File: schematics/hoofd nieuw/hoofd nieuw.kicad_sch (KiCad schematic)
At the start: 21 parts, among them J1 Conn_01x04_Pin

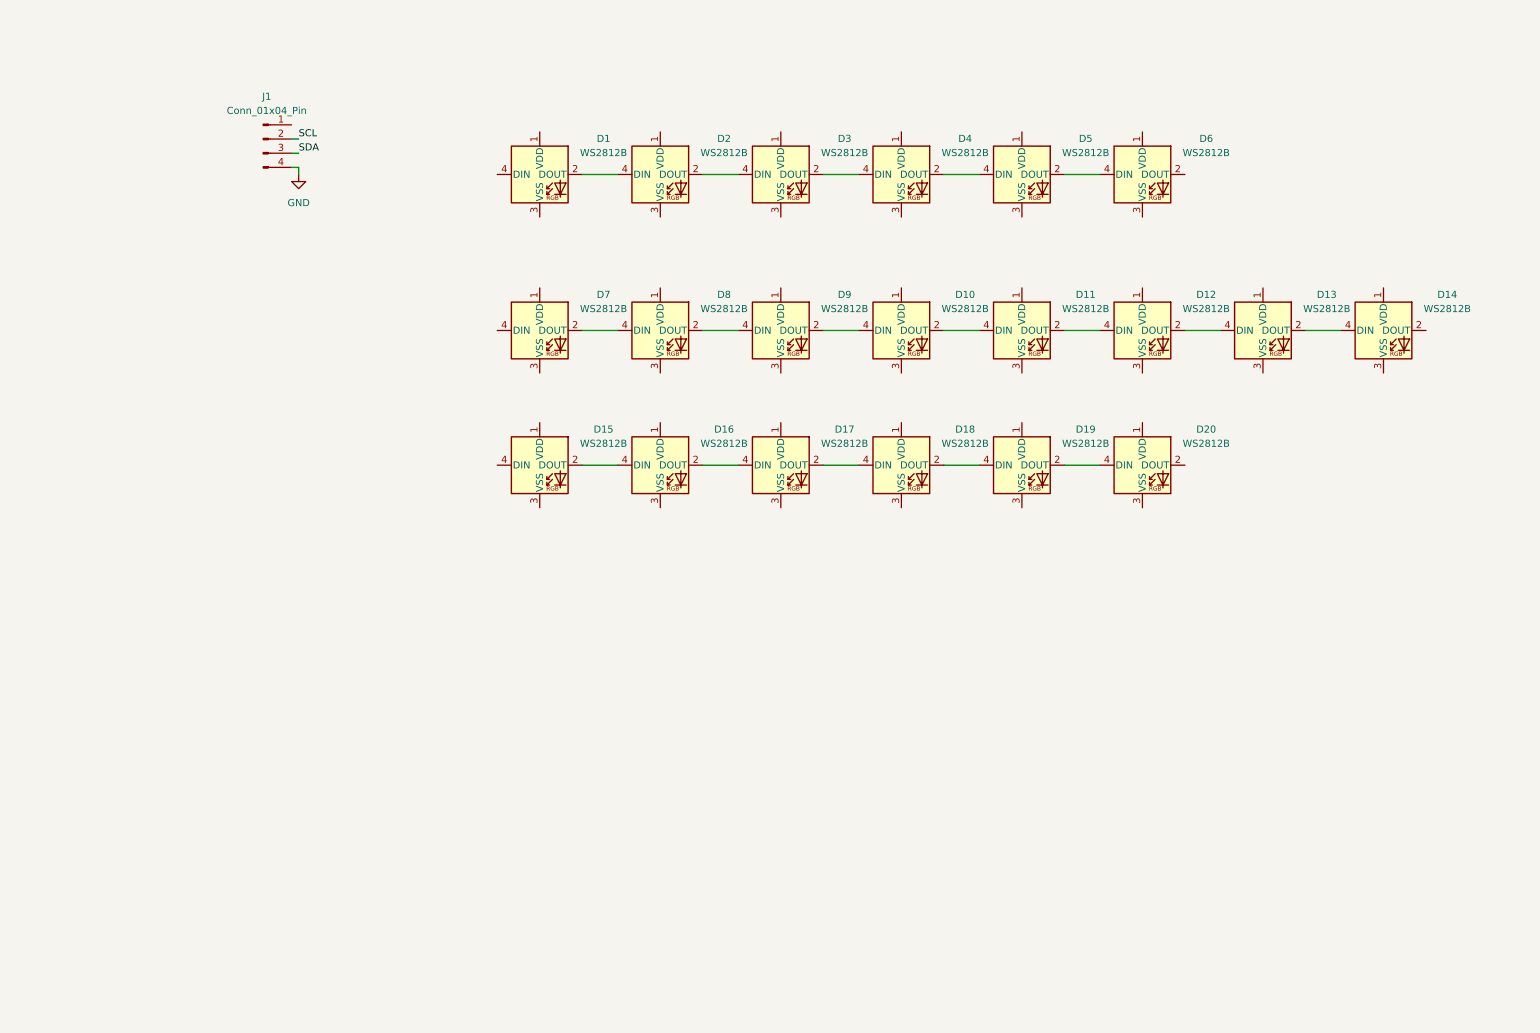
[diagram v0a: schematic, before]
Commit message: schema geupdate voor ATtiny 202 (nog niet af)
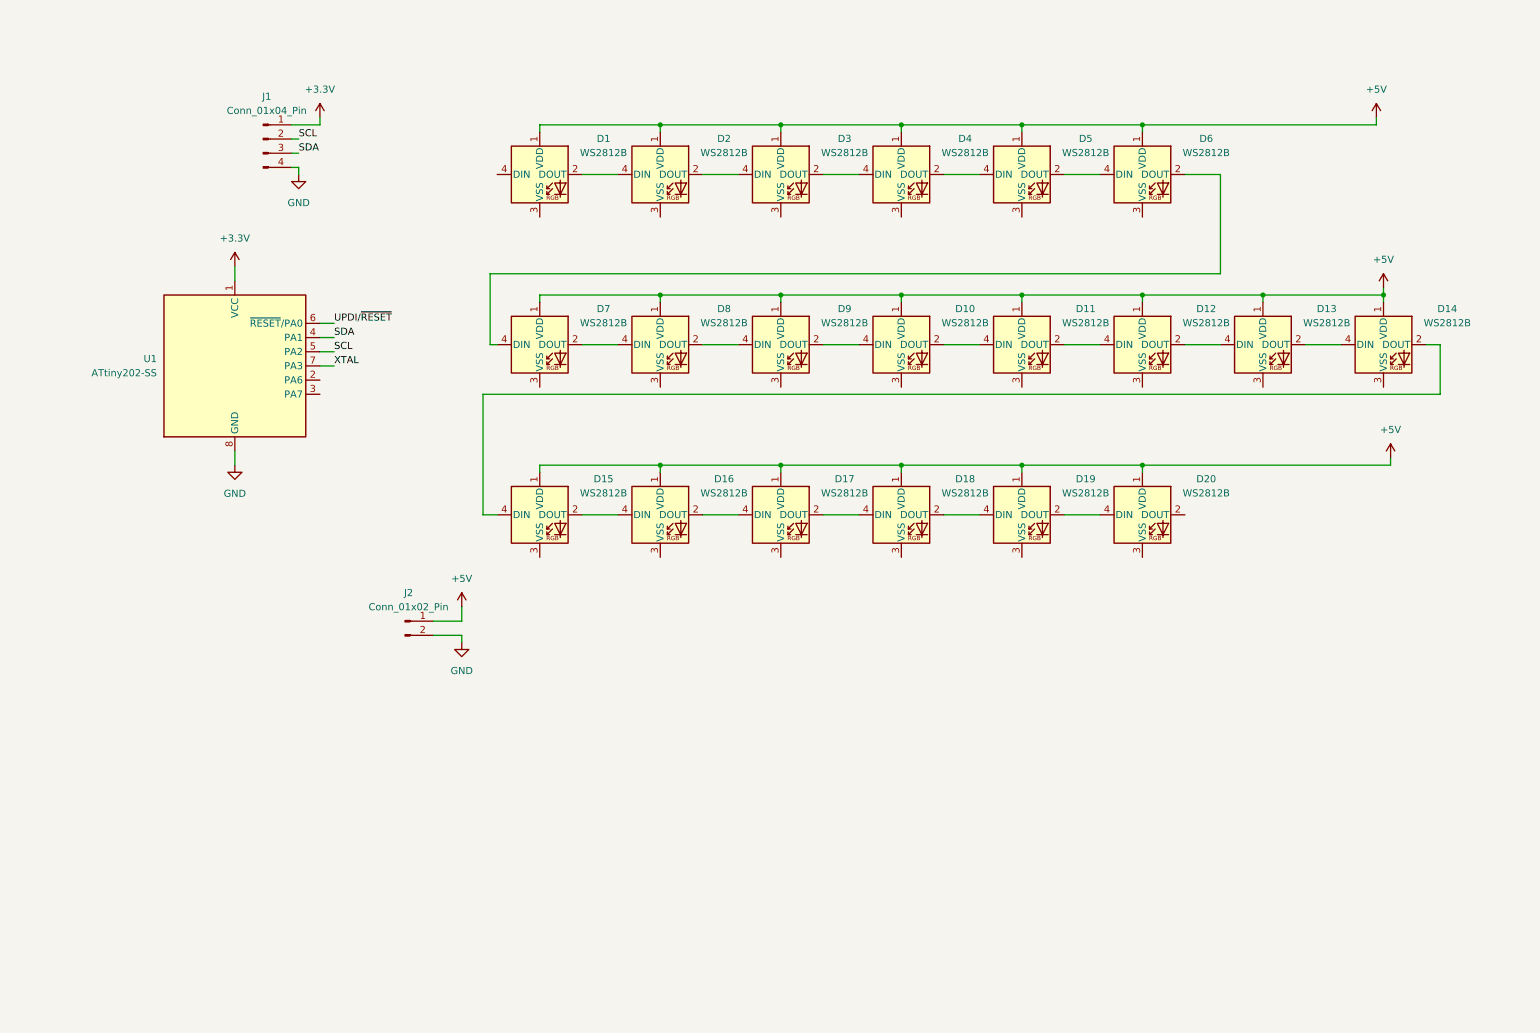
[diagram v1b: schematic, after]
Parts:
- added J2: Conn_01x02_Pin, symbol Connector:Conn_01x02_Pin
- added U1: ATtiny202-SS, Package_SO:SOIC-8_3.9x4.9mm_P1.27mm, symbol MCU_Microchip_ATtiny:ATtiny202-SS
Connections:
- net GND: now also J2.2 (Pin_2), U1.8 (GND)
- net SCL: now also U1.5 (PA2)
- net SDA: now also U1.4 (PA1)
- net +5V: now reaches D9.1 (VDD)
- net +5V: now also D1.1 (VDD), D10.1 (VDD), D11.1 (VDD), D12.1 (VDD), D13.1 (VDD), D14.1 (VDD), D15.1 (VDD), D16.1 (VDD), D17.1 (VDD), D18.1 (VDD), D19.1 (VDD), D2.1 (VDD), D20.1 (VDD), D3.1 (VDD), D4.1 (VDD), D5.1 (VDD), D6.1 (VDD), D7.1 (VDD), D8.1 (VDD), J2.1 (Pin_1)
- net at D15.4 (DIN): now also D14.2 (DOUT)
- net +3.3V: now reaches J1.1 (Pin_1)
- net +3.3V: now also U1.1 (VCC)
- net at D6.2 (DOUT): now also D7.4 (DIN)
- new net UPDI/~{RESET}: U1.6 (~{RESET}/PA0)
- new net XTAL: U1.7 (PA3)
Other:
- moved on the sheet: D10, D11, D12, D13, D14, D15, D16, D17, D18, D19, D20, D7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

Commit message: schema bijna klaar allen nog SRF02 toevoegen
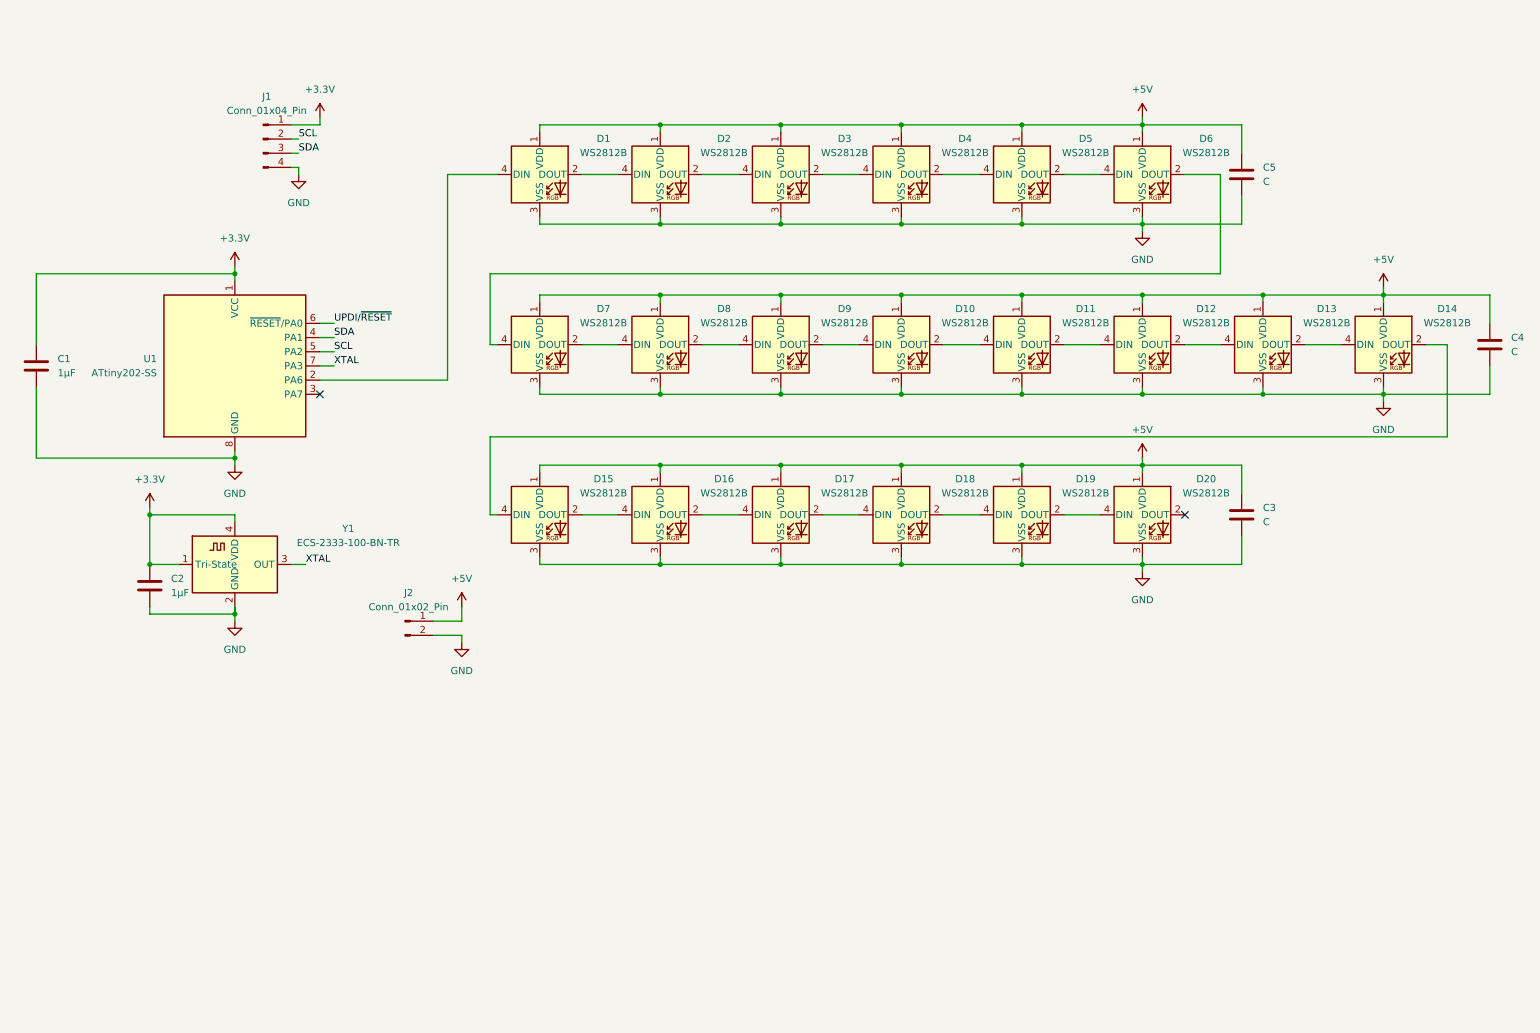
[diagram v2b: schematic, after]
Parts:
- added C1, C2: 1µF, symbol Device:C
- added C3, C4, C5: C, symbol Device:C
- added Y1: ECS-2333-100-BN-TR, Oscillator:Oscillator_SMD_ECS_2520MV-xxx-xx-4Pin_2.5x2.0mm, symbol Oscillator:ECS-2520MV-xxx-xx
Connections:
- net +3.3V: now also C1.1, C2.1, Y1.1 (Tri-State), Y1.4 (VDD)
- net +5V: now also C3.1, C4.1, C5.1
- net GND: now also D1.3 (VSS), D10.3 (VSS), D11.3 (VSS), D12.3 (VSS), D13.3 (VSS), D14.3 (VSS), D15.3 (VSS), D16.3 (VSS), D17.3 (VSS), D18.3 (VSS), D19.3 (VSS), D2.3 (VSS), D20.3 (VSS), D3.3 (VSS), D4.3 (VSS), D5.3 (VSS), D6.3 (VSS), D7.3 (VSS), D8.3 (VSS), D9.3 (VSS), C1.2, C2.2, C3.2, C4.2, C5.2, Y1.2 (GND)
- net XTAL: now also Y1.3 (OUT)
- net at D1.4 (DIN): now also U1.2 (PA6)
- no-connect marks 0 -> 2

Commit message: hoofdschema is af
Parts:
- removed Y1: ECS-2333-100-BN-TR, Oscillator:Oscillator_SMD_ECS_2520MV-xxx-xx-4Pin_2.5x2.0mm, symbol Oscillator:ECS-2520MV-xxx-xx
- added J3: SFR02, symbol Connector:Conn_01x05_Pin
- added J4: Conn_01x04_Pin, symbol Connector:Conn_01x04_Pin
- added Y1: ECS-2333MV-xxx-xx, Oscillator:Oscillator_SMD_ECS_2333MV-xxx-xx-4Pin_2.5x3.2mm, symbol robot:ECS-2333MV-xxx-xx
- C3, C4, C5: value C -> 1µF
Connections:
- net +3.3V: now also J3.1 (Pin_1), J4.4 (Pin_4), Y1.1 (Tri-State), Y1.4 (VDD); no longer C1.1, U1.1 (VCC)
- net GND: now also J3.5 (Pin_5), J4.1 (Pin_1), Y1.2 (GND)
- net SCL: now also J3.3 (Pin_3)
- net SDA: now also J3.2 (Pin_2)
- net UPDI/~{RESET}: now also J4.2 (Pin_2)
- net XTAL: now also Y1.3 (OUT)
- new net: C1.1, J4.3 (Pin_3), U1.1 (VCC)
- new net mode: J3.4 (Pin_4)
- no-connect marks 2 -> 3
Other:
- moved on the sheet: C3, C4, C5, D1, D10, D11, D12, D13, D14, D15, D16, D17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

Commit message: veranert de ATtiny202 naat ATtiny402 om genoeg opslag te hebben
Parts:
- U1: value ATtiny202-SS -> ATtiny402-SS
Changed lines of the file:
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@@
 			)
 		)
-		(property "Value" "ATtiny202-SS"
+		(property "Value" "ATtiny402-SS"
 			(at 43.18 81.2799 0)
 			(effects

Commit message: voeg de lichtsensor toe aan het hoofd
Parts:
- added C6, C7, C8: 1µF, symbol Device:C
- added R1: 10k, symbol Device:R
- added U2, U3: BH1750FVI-TR, BH1750FVI-TR:XDCR_BH1750FVI-TR, symbol BH1750FVI-TR:BH1750FVI-TR
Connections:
- net +3.3V: now also C7.1, C8.1, R1.1, U2.1 (VCC), U3.1 (VCC), U3.2 (ADDR)
- net GND: now also C6.2, C7.2, C8.2, U2.2 (ADDR), U2.3 (GND), U3.3 (GND)
- net SCL: now also U2.6 (SCL), U3.6 (SCL)
- net SDA: now also U2.4 (SDA), U3.4 (SDA)
- new net: C6.1, R1.2, U2.5 (DVI), U3.5 (DVI)
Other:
- note added: "de reset vertragen met ongeveer 10ms>>1µs verijst in de datascheet"

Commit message: teken de outline van het hoofd, en plaats de SRF02 (locatie gevoelig)
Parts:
- added D21: GS1M_R1_00001, Diode_SMD:D_SMA, symbol Device:D
- added R2: 10k, Resistor_SMD:R_0603_1608Metric, symbol Device:R
- C1, C2, C3, C4, C5, C6, C7, C8: footprint (none) -> Capacitor_SMD:C_0603_1608Metric
- J1, J4: footprint (none) -> Connector_PinHeader_2.54mm:PinHeader_1x04_P2.54mm_Vertical
- J2: footprint (none) -> Connector_PinHeader_2.54mm:PinHeader_1x02_P2.54mm_Vertical
- J3: footprint (none) -> Connector_PinHeader_2.54mm:PinHeader_1x05_P2.54mm_Vertical
- R1: footprint (none) -> Resistor_SMD:R_0603_1608Metric
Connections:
- net +5V: now also R2.1
- net at U1.2 (PA6): now also D21.1 (K); no longer D1.4 (DIN)
- new net: D1.4 (DIN), D21.2 (A), R2.2
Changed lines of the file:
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@@
 	)
 	(junction
+		(at 92.71 45.72)
+		(diameter 0)
+		(color 0 0 0 0)
+	)
+	(junction
 		(at 128.27 54.61)
 		(diameter 0)
@@
 	)
 	(junction
+		(at 106.68 36.83)
+		(diameter 0)
+		(color 255 0 0 1)
+	)
+	(junction
 		(at 214.63 67.31)
 		(diameter 0)
@@
 	(wire
 		(pts
+			(xy 92.71 62.23) (xy 92.71 82.55)
+		)
+		(stroke
+			(width 0)
+			(type default)
+		)
+	)
+	(wire
+		(pts
 			(xy 96.52 172.72) (xy 90.17 172.72)
 		)
@@
 	(wire
 		(pts
+			(xy 92.71 54.61) (xy 92.71 45.72)
+		)
+		(stroke
+			(width 0)
+			(type default)
+		)
+	)
+	(wire
+		(pts
 			(xy 214.63 53.34) (xy 214.63 54.61)
 		)
@@
 	(wire
 		(pts
-			(xy 72.39 82.55) (xy 95.25 82.55)
+			(xy 72.39 82.55) (xy 92.71 82.55)
 		)
 		(stroke
@@
 	(wire
 		(pts
+			(xy 106.68 36.83) (xy 92.71 36.83)
+		)
+		(stroke
+			(width 0)
+			(type default)
+			(color 255 0 0 1)
+		)
+	)
+	(wire
+		(pts
 			(xy 193.04 67.31) (xy 193.04 68.58)
 		)
@@
 	(wire
 		(pts
-			(xy 106.68 99.06) (xy 106.68 97.79)
+			(xy 92.71 45.72) (xy 99.06 45.72)
 		)
 		(stroke
 			(width 0)
 			(type default)
-			(color 255 0 0 1)
 		)
 	)
 	(wire
 		(pts
-			(xy 149.86 83.82) (xy 149.86 85.09)
+			(xy 106.68 99.06) (xy 106.68 97.79)
 		)
 		(stroke
 			(width 0)
 			(type default)
+			(color 255 0 0 1)
 		)
 	)
 	(wire
 		(pts
-			(xy 99.06 76.2) (xy 97.79 76.2)
+			(xy 149.86 83.82) (xy 149.86 85.09)
 		)
 		(stroke
@@
 	(wire
 		(pts
-			(xy 128.27 83.82) (xy 128.27 85.09)
+			(xy 99.06 76.2) (xy 97.79 76.2)
 		)
 		(stroke
@@
 	(wire
 		(pts
-			(xy 95.25 45.72) (xy 99.06 45.72)
+			(xy 128.27 83.82) (xy 128.27 85.09)
 		)
 		(stroke
@@
 	(wire
 		(pts
+			(xy 92.71 44.45) (xy 92.71 45.72)
+		)
+		(stroke
+			(width 0)
+			(type default)
+		)
+	)
+	(wire
+		(pts
 			(xy 67.31 115.57) (xy 69.85 115.57)
 		)
@@
 	(wire
 		(pts
-			(xy 95.25 82.55) (xy 95.25 45.72)
-		)
-		(stroke
-			(width 0)
-			(type default)
-		)
-	)
-	(wire
-		(pts
 			(xy 134.62 153.67) (xy 134.62 166.37)
 		)
@@
 			)
 		)
-		(property "Footprint" ""
+		(property "Footprint" "Connector_PinHeader_2.54mm:PinHeader_1x02_P2.54mm_Vertical"
 			(at 25.4 25.4 0)
 			(effects
@@
 			)
 		)
-		(property "Footprint" ""
+		(property "Footprint" "Capacitor_SMD:C_0603_1608Metric"
 			(at 277.8252 80.01 0)
 			(effects
@@
 	)
 	(symbol
+		(lib_id "Device:D")
+		(at 92.71 58.42 90)
+		(unit 1)
+		(exclude_from_sim no)
+		(in_bom yes)
+		(on_board yes)
+		(dnp no)
+		(fields_autoplaced yes)
+		(property "Reference" "D21"
+			(at 95.25 57.1499 90)
+			(effects
+				(font
+					(size 1.27 1.27)
+				)
+				(justify right)
+			)
+		)
+		(property "Value" "GS1M_R1_00001"
+			(at 95.25 59.6899 90)
+			(effects
+				(font
+					(size 1.27 1.27)
+				)
+				(justify right)
+			)
+		)
+		(property "Footprint" "Diode_SMD:D_SMA"
+			(at 92.71 58.42 0)
+			(effects
+				(font
+					(size 1.27 1.27)
+				)
+				(hide yes)
+			)
+		)
+		(property "Datasheet" "~"
+			(at 92.71 58.42 0)
+			(effects
+				(font
+					(size 1.27 1.27)
+				)
+				(hide yes)
+			)
+		)
+		(property "Description" "Diode"
+			(at 92.71 58.42 0)
+			(effects
+				(font
+					(size 1.27 1.27)
+				)
+				(hide yes)
+			)
+		)
+		(property "Sim.Device" "D"
+			(at 92.71 58.42 0)
+			(effects
+				(font
+					(size 1.27 1.27)
+				)
+				(hide yes)
+			)
+		)
+		(property "Sim.Pins" "1=K 2=A"
+			(at 92.71 58.42 0)
+			(effects
+				(font
+					(size 1.27 1.27)
+				)
+				(hide yes)
+			)
+		)
+		(pin "2"
+		)
+		(pin "1"
+		)
+		(instances
+			(project ""
+				(path "/7e0a6d27-e85c-4a07-8035-4491285a0fea"
+					(reference "D21")
+					(unit 1)
+				)
+			)
+		)
+	)
+	(symbol
 		(lib_id "LED:WS2812B")
 		(at 149.86 76.2 0)
@@
 			)
 		)
-		(property "Footprint" ""
+		(property "Footprint" "Capacitor_SMD:C_0603_1608Metric"
 			(at 22.5552 83.82 0)
 			(effects
@@
 			)
 		)
-		(property "Footprint" ""
+		(property "Footprint" "Connector_PinHeader_2.54mm:PinHeader_1x04_P2.54mm_Vertical"
 			(at 44.45 27.94 0)
 			(effects
@@
 			)
 		)
-		(property "Footprint" ""
+		(property "Footprint" "Connector_PinHeader_2.54mm:PinHeader_1x04_P2.54mm_Vertical"
 			(at 59.69 48.26 0)
 			(effects
@@
 			)
 		)
-		(property "Footprint" ""
+		(property "Footprint" "Capacitor_SMD:C_0603_1608Metric"
 			(at 127.9652 181.61 0)
 			(effects
@@
 			)
 		)
-		(property "Footprint" ""
+		(property "Footprint" "Capacitor_SMD:C_0603_1608Metric"
 			(at 233.3752 110.49 0)
 			(effects
@@
 			)
 		)
-		(property "Footprint" ""
+		(property "Footprint" "Capacitor_SMD:C_0603_1608Metric"
 			(at 42.8752 123.19 0)
 			(effects
@@
 			)
 		)
-		(property "Footprint" ""
+		(property "Footprint" "Capacitor_SMD:C_0603_1608Metric"
 			(at 233.3752 49.53 0)
 			(effects
@@
 			)
 		)
-		(property "Footprint" ""
+		(property "Footprint" "Connector_PinHeader_2.54mm:PinHeader_1x05_P2.54mm_Vertical"
 			(at 64.77 30.48 0)
 			(effects
@@
 			)
 		)
-		(property "Footprint" ""
+		(property "Footprint" "Resistor_SMD:R_0603_1608Metric"
 			(at 141.732 151.13 90)
 			(effects
@@
 			)
 		)
-		(property "Footprint" ""
+		(property "Footprint" "Capacitor_SMD:C_0603_1608Metric"
 			(at 127.9652 143.51 0)
 			(effects
@@
 	)
 	(symbol
+		(lib_id "Device:R")
+		(at 92.71 40.64 0)
+		(unit 1)
+		(exclude_from_sim no)
+		(in_bom yes)
+		(on_board yes)
+		(dnp no)
+		(fields_autoplaced yes)
+		(property "Reference" "R2"
+			(at 95.25 39.3699 0)
+			(effects
+				(font
+					(size 1.27 1.27)
+				)
+				(justify left)
+			)
+		)
+		(property "Value" "10k"
+			(at 95.25 41.9099 0)
+			(effects
+				(font
+					(size 1.27 1.27)
+				)
+				(justify left)
+			)
+		)
+		(property "Footprint" "Resistor_SMD:R_0603_1608Metric"
+			(at 90.932 40.64 90)
+			(effects
+				(font
+					(size 1.27 1.27)
+				)
+				(hide yes)
+			)
+		)
+		(property "Datasheet" "~"
+			(at 92.71 40.64 0)
+			(effects
+				(font
+					(size 1.27 1.27)
+				)
+				(hide yes)
+			)
+		)
+		(property "Description" "Resistor"
+			(at 92.71 40.64 0)
+			(effects
+				(font
+					(size 1.27 1.27)
+				)
+				(hide yes)
+			)
+		)
+		(pin "1"
+		)
+		(pin "2"
+		)
+		(instances
+			(project "hoofd nieuw"
+				(path "/7e0a6d27-e85c-4a07-8035-4491285a0fea"
+					(reference "R2")
+					(unit 1)
+				)
+			)
+		)
+	)
+	(symbol
 		(lib_id "LED:WS2812B")
 		(at 193.04 106.68 0)
@@
 			)
 		)
-		(property "Footprint" ""
+		(property "Footprint" "Capacitor_SMD:C_0603_1608Metric"
 			(at 144.4752 165.1 0)
 			(effects
